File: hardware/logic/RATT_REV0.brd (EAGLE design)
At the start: 127 x 76.2 mm, 126 parts, among them IC1 TLP292-4, IC13 MCP73831, IC16 PCA9539PW, IC2 CPC1002N, IC3 CPC1002N, IC4 CPC1002N, IC5 CPC1002N, J1 4P-2.0, J2 4P-2.0, J3 F-1X06-SIP-100-40, J4 4P-2.0, J6 4P-2.0, J7 PHOENIX1803484, J8 PHOENIX1803484, Q1 2.5A/30V, Q2 MBT3904DW1T1, Q3 2.5A/30V, Q5 2N7002, Q6 2.5A/30V, U1 RPI-ZERO, U5 AP2112K-3.3V

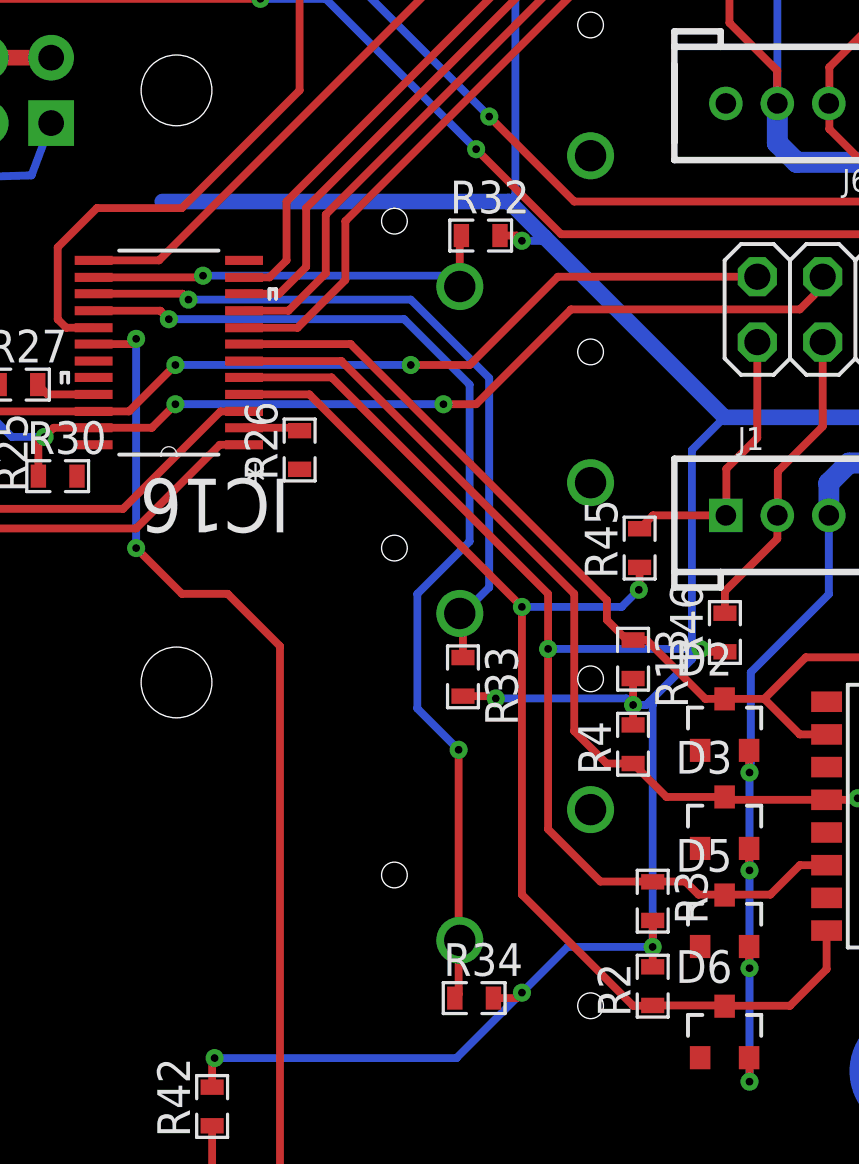
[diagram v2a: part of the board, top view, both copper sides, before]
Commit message: Fixed some derps
Routed through a few mounting areas, fixed that.
Removed file name from the imported bmp files in the library and on the board
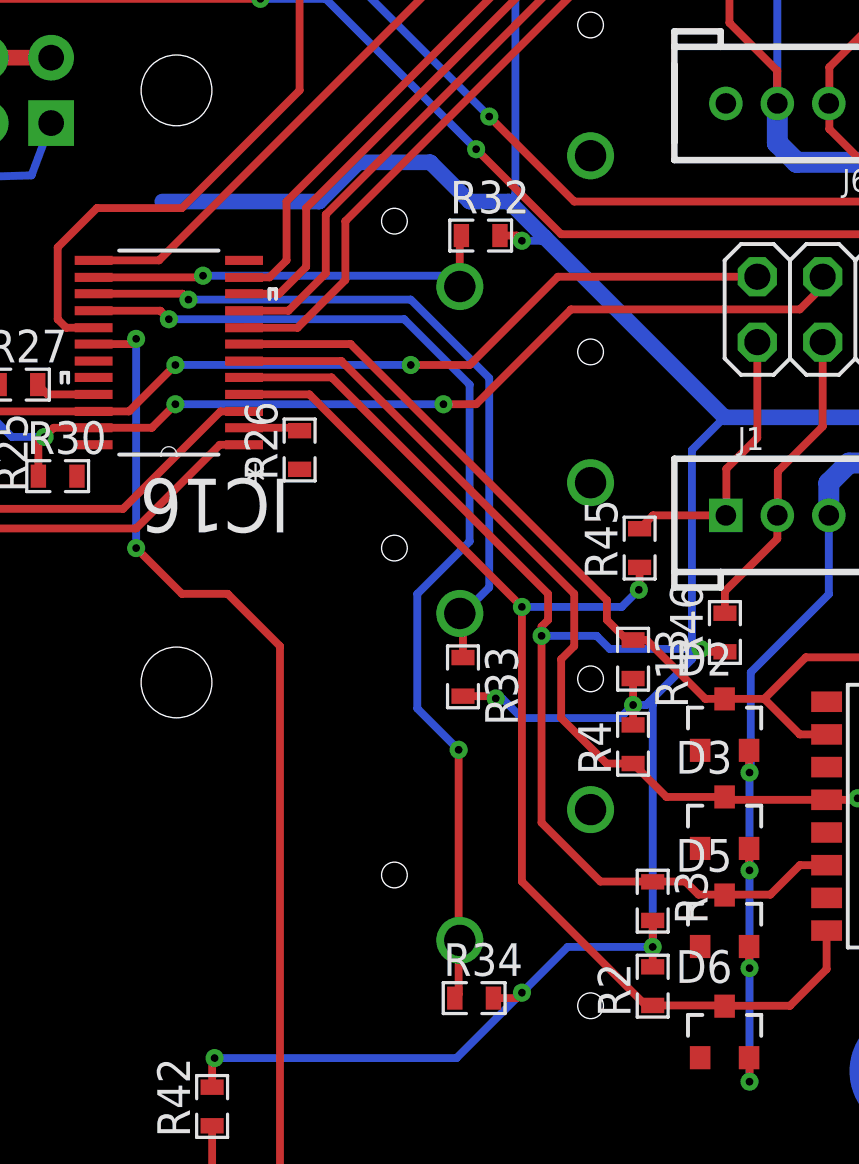
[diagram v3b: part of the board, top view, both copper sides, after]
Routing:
- net +3V3: track 109.1 -> 110.7 mm
- net IN1: track 43.7 -> 44.7 mm
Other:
- board text removed: "C:/Users/Adam/Documents/GitHub/ratt/hardware/references/oshw-logo_bw.bmp"
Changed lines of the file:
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@@
 <layer number="23" name="tOrigins" color="15" fill="1" visible="yes" active="yes"/>
 <layer number="24" name="bOrigins" color="15" fill="1" visible="yes" active="yes"/>
-<layer number="25" name="tNames" color="7" fill="1" visible="no" active="yes"/>
-<layer number="26" name="bNames" color="7" fill="1" visible="no" active="yes"/>
-<layer number="27" name="tValues" color="7" fill="1" visible="no" active="yes"/>
-<layer number="28" name="bValues" color="7" fill="1" visible="no" active="yes"/>
-<layer number="29" name="tStop" color="7" fill="3" visible="no" active="yes"/>
-<layer number="30" name="bStop" color="7" fill="6" visible="no" active="yes"/>
-<layer number="31" name="tCream" color="7" fill="4" visible="no" active="yes"/>
-<layer number="32" name="bCream" color="7" fill="5" visible="no" active="yes"/>
+<layer number="25" name="tNames" color="7" fill="1" visible="yes" active="yes"/>
+<layer number="26" name="bNames" color="7" fill="1" visible="yes" active="yes"/>
+<layer number="27" name="tValues" color="7" fill="1" visible="yes" active="yes"/>
+<layer number="28" name="bValues" color="7" fill="1" visible="yes" active="yes"/>
+<layer number="29" name="tStop" color="7" fill="3" visible="yes" active="yes"/>
+<layer number="30" name="bStop" color="7" fill="6" visible="yes" active="yes"/>
+<layer number="31" name="tCream" color="7" fill="4" visible="yes" active="yes"/>
+<layer number="32" name="bCream" color="7" fill="5" visible="yes" active="yes"/>
 <layer number="33" name="tFinish" color="6" fill="3" visible="yes" active="yes"/>
 <layer number="34" name="bFinish" color="6" fill="6" visible="yes" active="yes"/>
@@
 <layer number="49" name="Reference" color="7" fill="1" visible="yes" active="yes"/>
 <layer number="50" name="dxf" color="7" fill="1" visible="no" active="no"/>
-<layer number="51" name="tDocu" color="17" fill="1" visible="no" active="yes"/>
-<layer number="52" name="bDocu" color="19" fill="1" visible="no" active="yes"/>
+<layer number="51" name="tDocu" color="17" fill="1" visible="yes" active="yes"/>
+<layer number="52" name="bDocu" color="19" fill="1" visible="yes" active="yes"/>
 <layer number="53" name="tGND_GNDA" color="7" fill="9" visible="no" active="no"/>
 <layer number="54" name="bGND_GNDA" color="1" fill="9" visible="no" active="no"/>
@@
 <rectangle x1="57.3405" y1="-21.6027" x2="59.0169" y2="-21.5773" layer="200"/>
 <rectangle x1="57.3659" y1="-21.5773" x2="58.9915" y2="-21.5519" layer="200"/>
-<text x="50.5714" y="-37.6936" size="0.0508" layer="200" font="vector">C:/Users/Adam/Documents/GitHub/ratt/hardware/references/oshw-logo_bw.bmp</text>
 <rectangle x1="87.148" y1="37.846" x2="115.068" y2="46.736" layer="51"/>
 </plain>
@@
 <wire x1="90.932" y1="38.1" x2="83.947" y2="45.085" width="0.6096" layer="16"/>
 <wire x1="83.947" y1="45.085" x2="82.55" y2="46.482" width="0.6096" layer="16"/>
-<wire x1="82.55" y1="46.482" x2="69.088" y2="46.482" width="0.6096" layer="16"/>
 <wire x1="90.932" y1="38.1" x2="89.662" y2="36.83" width="0.3048" layer="16"/>
 <wire x1="89.662" y1="36.83" x2="89.662" y2="28.702" width="0.3048" layer="16"/>
@@
 <wire x1="81.952" y1="27.268" x2="82.042" y2="27.178" width="0.3048" layer="1"/>
 <via x="82.042" y="27.178" extent="1-16" drill="0.3"/>
-<wire x1="82.042" y1="27.178" x2="87.122" y2="27.178" width="0.3048" layer="16"/>
-<wire x1="87.122" y1="27.178" x2="87.376" y2="26.924" width="0.3048" layer="16"/>
 <wire x1="82.206" y1="45.16" x2="82.856" y2="45.16" width="0.3048" layer="1"/>
 <wire x1="82.856" y1="45.16" x2="83.058" y2="44.958" width="0.3048" layer="1"/>
@@
 <wire x1="82.804" y1="57.912" x2="82.804" y2="46.736" width="0.3048" layer="16"/>
 <wire x1="82.804" y1="46.736" x2="82.55" y2="46.482" width="0.3048" layer="16"/>
+<wire x1="82.55" y1="46.482" x2="81.026" y2="46.482" width="0.6096" layer="16"/>
+<wire x1="81.026" y1="46.482" x2="79.502" y2="48.006" width="0.6096" layer="16"/>
+<wire x1="79.502" y1="48.006" x2="76.708" y2="48.006" width="0.6096" layer="16"/>
+<wire x1="76.708" y1="48.006" x2="75.184" y2="46.482" width="0.6096" layer="16"/>
+<wire x1="75.184" y1="46.482" x2="69.088" y2="46.482" width="0.6096" layer="16"/>
+<wire x1="82.042" y1="27.178" x2="82.296" y2="27.178" width="0.3048" layer="16"/>
+<wire x1="82.296" y1="27.178" x2="83.058" y2="26.416" width="0.3048" layer="16"/>
+<wire x1="83.058" y1="26.416" x2="86.868" y2="26.416" width="0.3048" layer="16"/>
+<wire x1="86.868" y1="26.416" x2="87.376" y2="26.924" width="0.3048" layer="16"/>
 <wire x1="53.5814" y1="67.9704" x2="66.636" y2="69.862" width="0" layer="19" extent="1-1"/>
 <wire x1="53.142" y1="70.2652" x2="53.5814" y2="67.9704" width="0" layer="19" extent="1-1"/>
@@
 <wire x1="90.948" y1="15.24" x2="90.932" y2="15.224" width="0.3048" layer="1"/>
 <wire x1="94.894" y1="18.161" x2="94.894" y2="16.662" width="0.3048" layer="1"/>
-<wire x1="83.058" y1="19.558" x2="83.058" y2="30.734" width="0.3048" layer="1"/>
+<wire x1="83.058" y1="20.066" x2="83.058" y2="30.734" width="0.3048" layer="1"/>
 <via x="83.058" y="30.734" extent="1-16" drill="0.3"/>
 <wire x1="87.63" y1="32.27" x2="87.63" y2="31.43" width="0.3048" layer="1"/>
@@
 <wire x1="86.934" y1="30.734" x2="83.058" y2="30.734" width="0.3048" layer="16"/>
 <wire x1="93.472" y1="15.24" x2="94.894" y2="16.662" width="0.3048" layer="1"/>
-<wire x1="83.058" y1="19.558" x2="87.376" y2="15.24" width="0.3048" layer="1"/>
-<wire x1="87.376" y1="15.24" x2="88.126" y2="15.24" width="0.3048" layer="1"/>
 <wire x1="88.126" y1="15.24" x2="88.138" y2="15.252" width="0.3048" layer="1"/>
 <wire x1="88.138" y1="15.252" x2="90.904" y2="15.252" width="0.3048" layer="1"/>
 <wire x1="90.904" y1="15.252" x2="90.932" y2="15.224" width="0.3048" layer="1"/>
+<wire x1="88.126" y1="15.24" x2="87.884" y2="15.24" width="0.3048" layer="1"/>
+<wire x1="87.884" y1="15.24" x2="83.058" y2="20.066" width="0.3048" layer="1"/>
 </signal>
 <signal name="IN1">
@@
 <wire x1="88.15" y1="20.066" x2="88.138" y2="20.054" width="0.3048" layer="1"/>
 <wire x1="88.15" y1="20.066" x2="86.106" y2="20.066" width="0.3048" layer="1"/>
-<wire x1="86.106" y1="20.066" x2="84.074" y2="22.098" width="0.3048" layer="1"/>
-<wire x1="84.074" y1="22.098" x2="84.074" y2="29.102" width="0.3048" layer="1"/>
-<wire x1="84.074" y1="29.102" x2="84.074" y2="31.242" width="0.3048" layer="1"/>
+<wire x1="86.106" y1="20.066" x2="83.82" y2="22.352" width="0.3048" layer="1"/>
+<wire x1="83.82" y1="22.352" x2="83.82" y2="29.61" width="0.3048" layer="1"/>
 <wire x1="84.074" y1="31.242" x2="75.6666" y2="39.6494" width="0.3048" layer="1"/>
-<via x="84.074" y="29.102" extent="1-16" drill="0.3"/>
+<via x="83.82" y="29.61" extent="1-16" drill="0.3"/>
 <wire x1="90.944" y1="28.99" x2="90.11" y2="28.99" width="0.3048" layer="1"/>
 <wire x1="90.11" y1="28.99" x2="90" y2="29.1" width="0.3048" layer="1"/>
 <via x="90" y="29.1" extent="1-16" drill="0.3"/>
-<wire x1="90" y1="29.1" x2="84.076" y2="29.1" width="0.3048" layer="16"/>
-<wire x1="84.076" y1="29.1" x2="84.074" y2="29.102" width="0.3048" layer="16"/>
+<wire x1="84.076" y1="29.608" x2="83.82" y2="29.61" width="0.3048" layer="16"/>
+<wire x1="90" y1="29.1" x2="86.47" y2="29.1" width="0.3048" layer="16"/>
+<wire x1="86.47" y1="29.1" x2="85.96" y2="29.61" width="0.3048" layer="16"/>
+<wire x1="83.82" y1="29.61" x2="85.96" y2="29.61" width="0.3048" layer="16"/>
+<wire x1="83.82" y1="29.61" x2="83.82" y2="29.972" width="0.3048" layer="1"/>
+<wire x1="83.82" y1="29.972" x2="84.074" y2="30.226" width="0.3048" layer="1"/>
+<wire x1="84.074" y1="30.226" x2="84.074" y2="31.242" width="0.3048" layer="1"/>
 </signal>
 <signal name="IN2">
@@
 <wire x1="94.894" y1="23.241" x2="91.043" y2="23.241" width="0.3048" layer="1"/>
 <wire x1="91.043" y1="23.241" x2="90.932" y2="23.352" width="0.3048" layer="1"/>
-<wire x1="85.09" y1="25.908" x2="85.09" y2="31.242" width="0.3048" layer="1"/>
 <wire x1="87.376" y1="24.65" x2="88.674" y2="23.352" width="0.3048" layer="1"/>
 <wire x1="88.674" y1="23.352" x2="90.932" y2="23.352" width="0.3048" layer="1"/>
-<wire x1="85.09" y1="25.908" x2="86.348" y2="24.65" width="0.3048" layer="1"/>
+<wire x1="84.582" y1="26.416" x2="86.348" y2="24.65" width="0.3048" layer="1"/>
 <wire x1="86.348" y1="24.65" x2="87.376" y2="24.65" width="0.3048" layer="1"/>
 <wire x1="99.434" y1="30.134" x2="98.734" y2="30.134" width="0.3048" layer="1"/>
@@
 <wire x1="96.041" y1="23.241" x2="94.894" y2="23.241" width="0.3048" layer="1"/>
 <wire x1="76.0476" y1="40.2844" x2="85.09" y2="31.242" width="0.3048" layer="1"/>
+<wire x1="84.582" y1="26.416" x2="84.582" y2="28.702" width="0.3048" layer="1"/>
+<wire x1="84.582" y1="28.702" x2="85.09" y2="29.21" width="0.3048" layer="1"/>
+<wire x1="85.09" y1="29.21" x2="85.09" y2="31.242" width="0.3048" layer="1"/>
 </signal>
 <signal name="IN3">

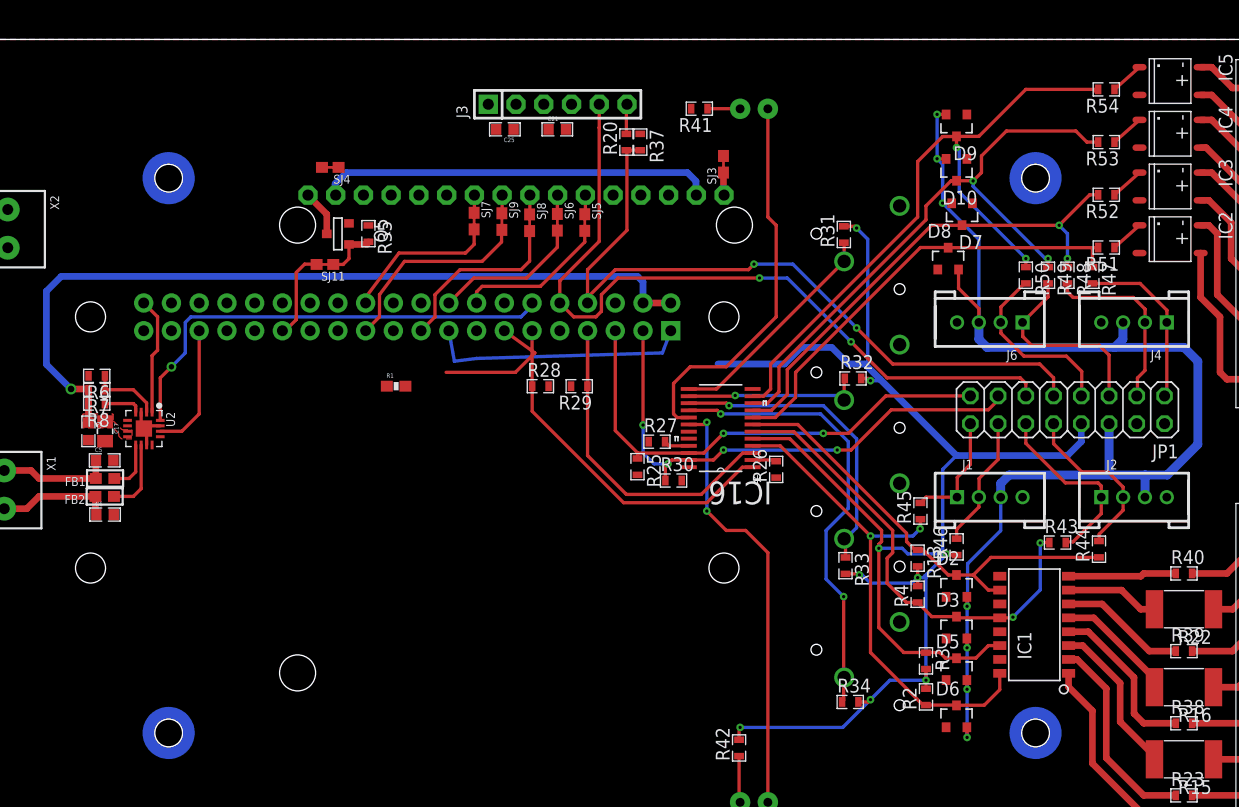
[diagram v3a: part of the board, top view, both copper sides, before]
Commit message: Ran DRC, fixed stuff
Ran a DRC on existing routing and fixed critical errors
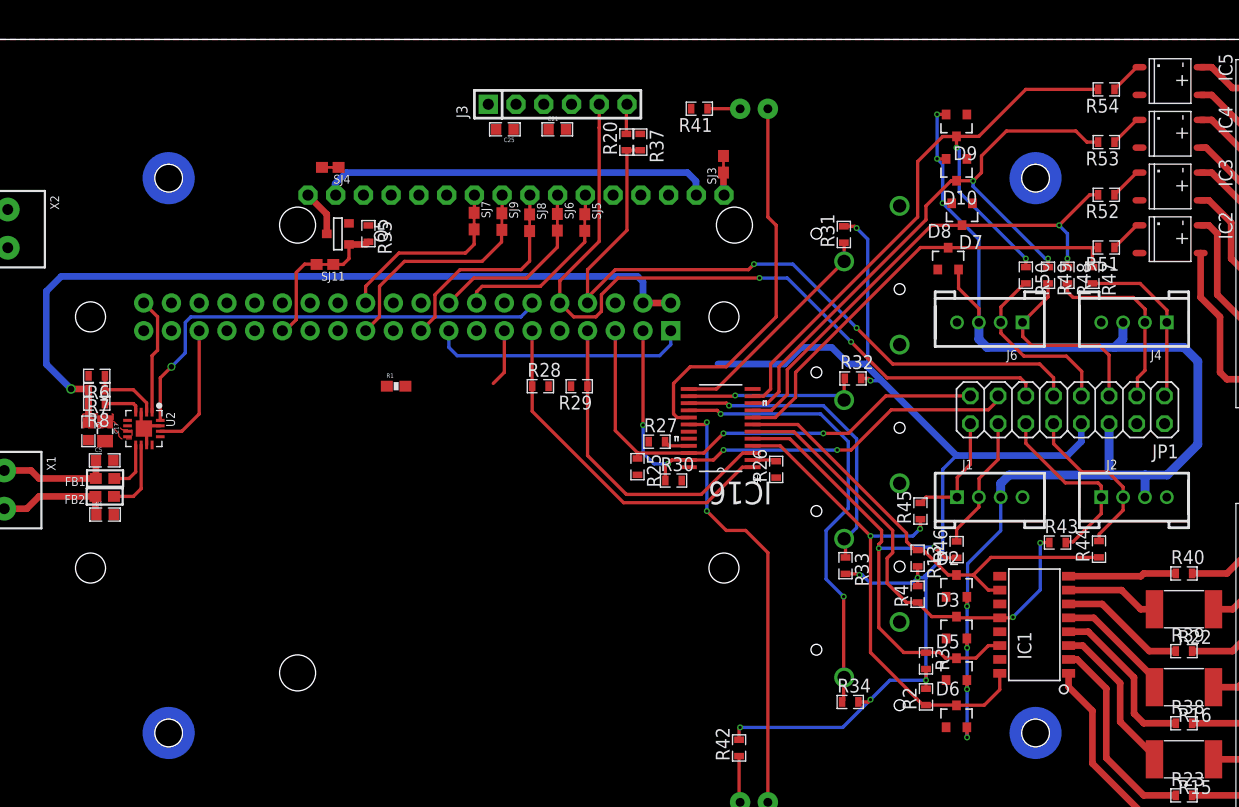
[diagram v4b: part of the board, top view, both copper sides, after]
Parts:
- moved R46 0.25 mm to (90.9, 29.5)
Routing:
- net !SHUTDOWN: track 12.3 -> 5.25 mm

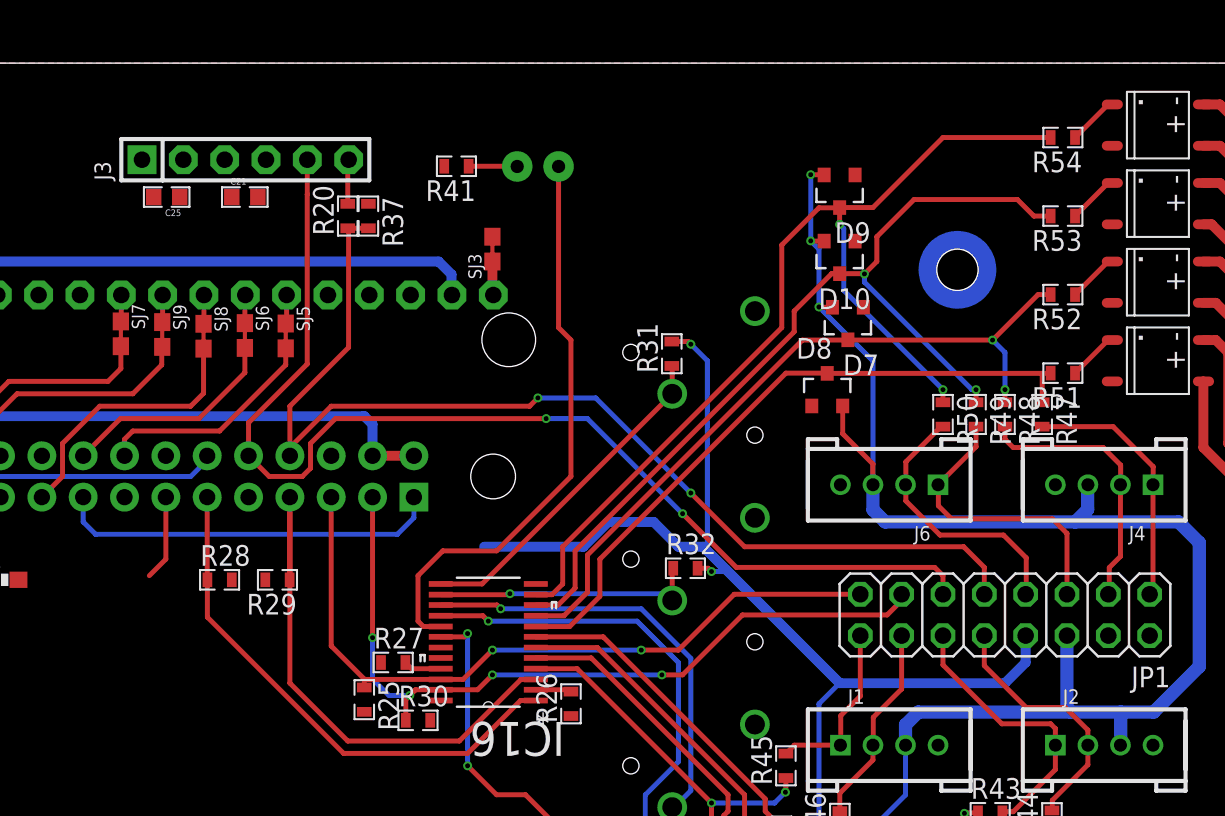
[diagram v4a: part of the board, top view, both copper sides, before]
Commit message: A few tweaks on sch and brd
added PU to unused IO, added caps and beads to RFID power lines
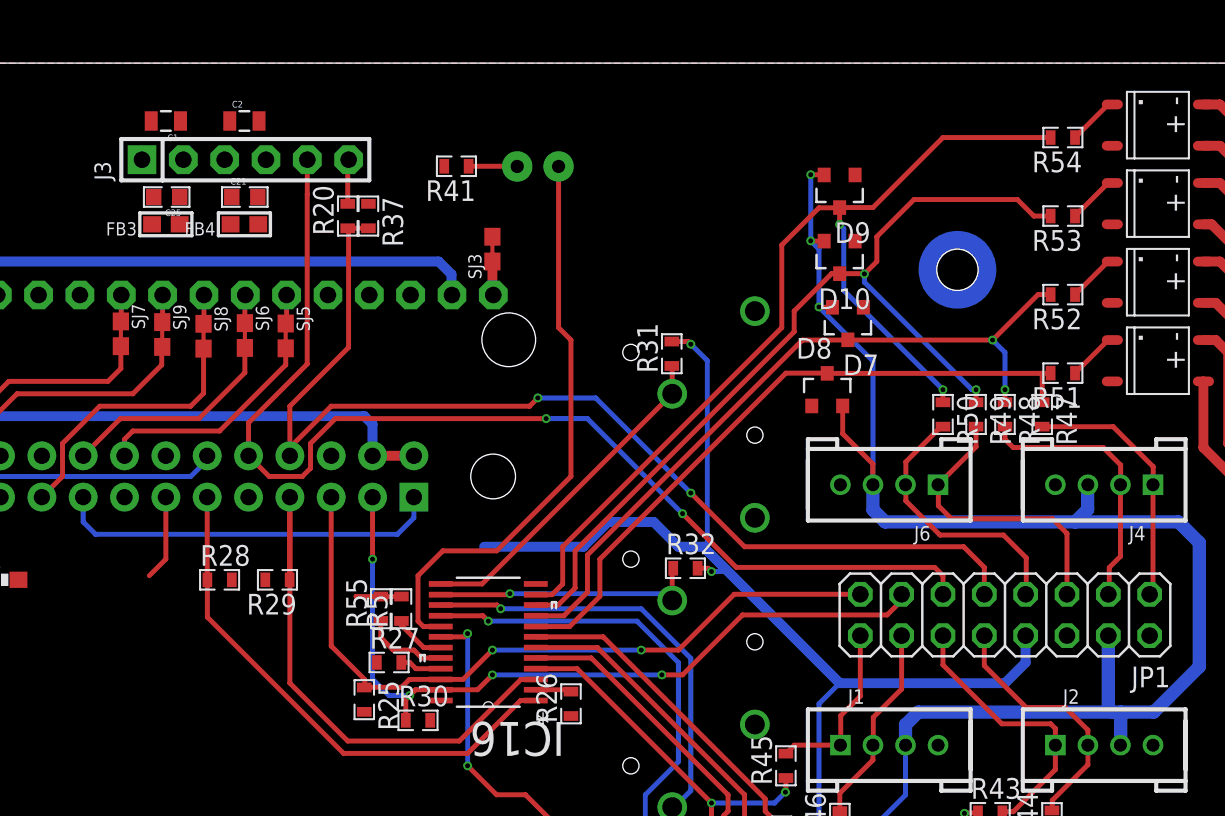
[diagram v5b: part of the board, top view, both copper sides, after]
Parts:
- added C1, C2: 10uF, SparkFun-Capacitors:0805@1
- added FB3, FB4: (no value), DURRIDGE-INDUCTORS:0603
- added R5, R55: 10K, MakeItLabs:0603-RES
- moved R27 0.25 mm to (63.2, 39.4)
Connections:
- new net N$13: IC16.19, R5.1
- new net N$50: C2.1, C21.1, FB4.1, J3.3
- new net N$51: C1.1, C25.1, FB3.1, J3.2
- new net N$8: IC16.20, R55.1
- net +3V3: now also FB4.2, R5.2, R55.2; no longer C21.1, J3.3
- net +5V: now also JP1.4; no longer JP1.6
- net GND: now also C1.2, C2.2, JP1.6; no longer JP1.4
- net V_USB: now also FB3.2; no longer C25.1, J3.2
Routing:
- net N$8: track 0.00 -> 5.23 mm
- net N$13: track 0.00 -> 3.25 mm
- net +3V3: track 110.7 -> 113.5 mm
